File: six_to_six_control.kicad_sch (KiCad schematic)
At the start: 16 parts, among them J1 relays, J2 relays, J3 relays, J4 relays, J5 relays, J6 relays, J7 12V Power, U1 RS-485_module

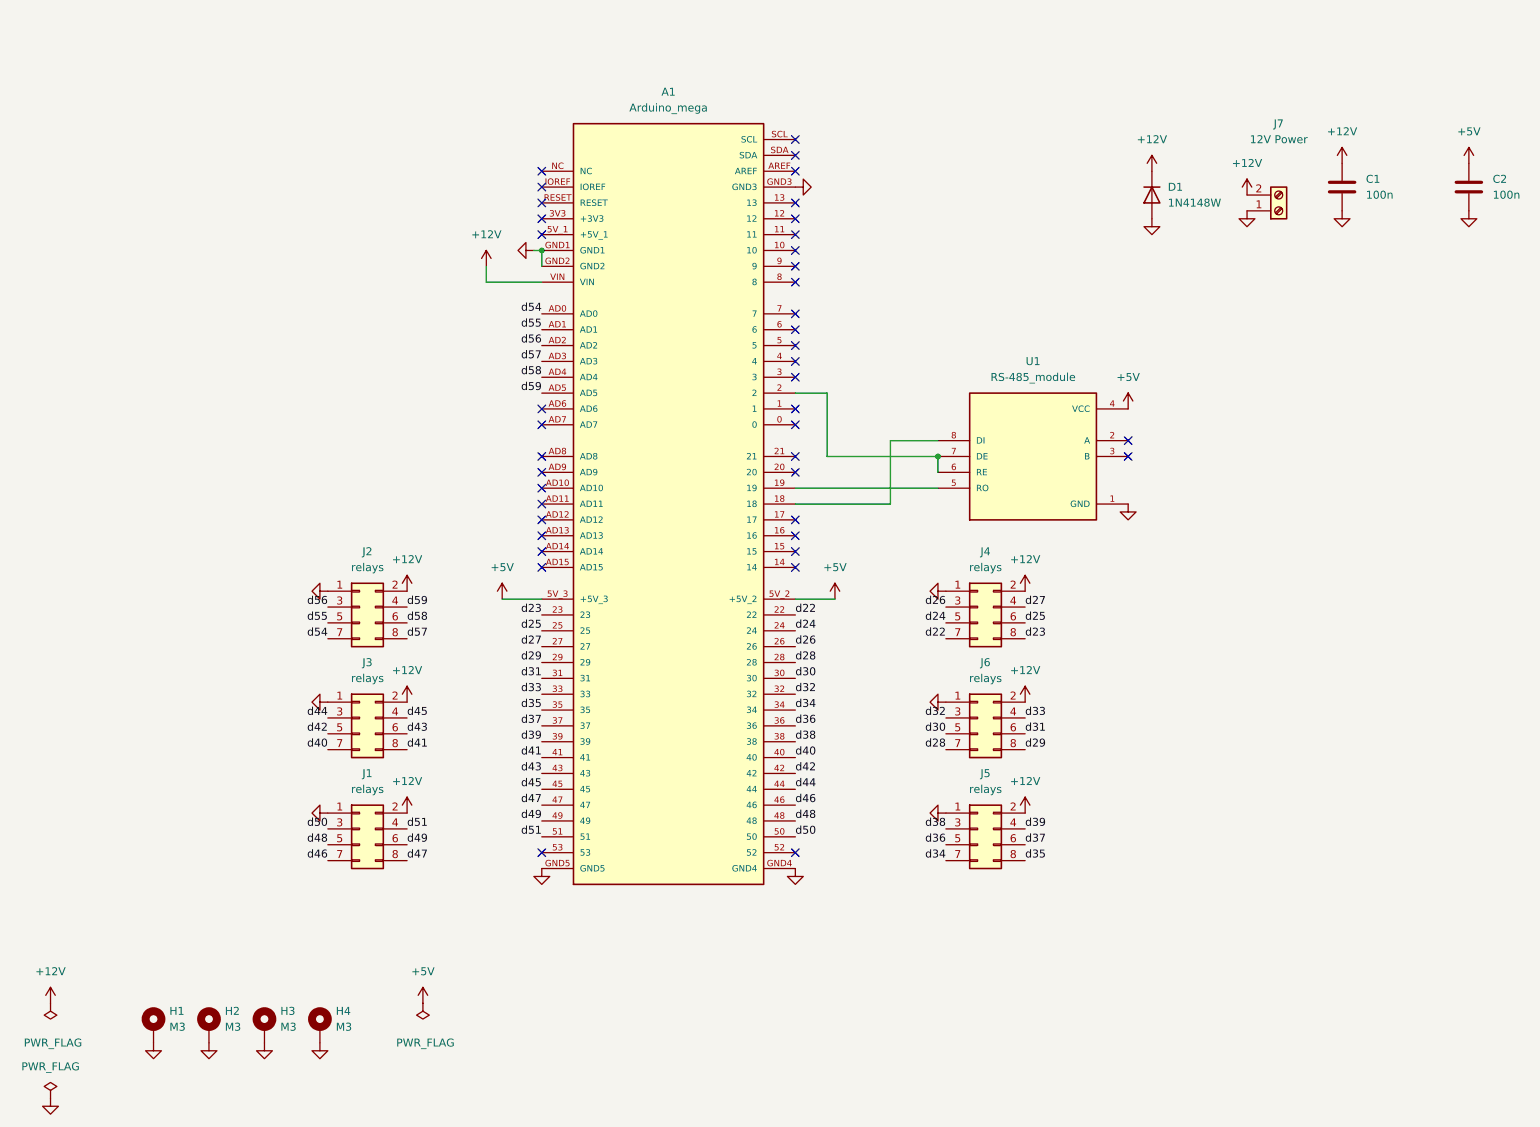
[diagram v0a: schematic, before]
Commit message: added db9 and Ethernet module
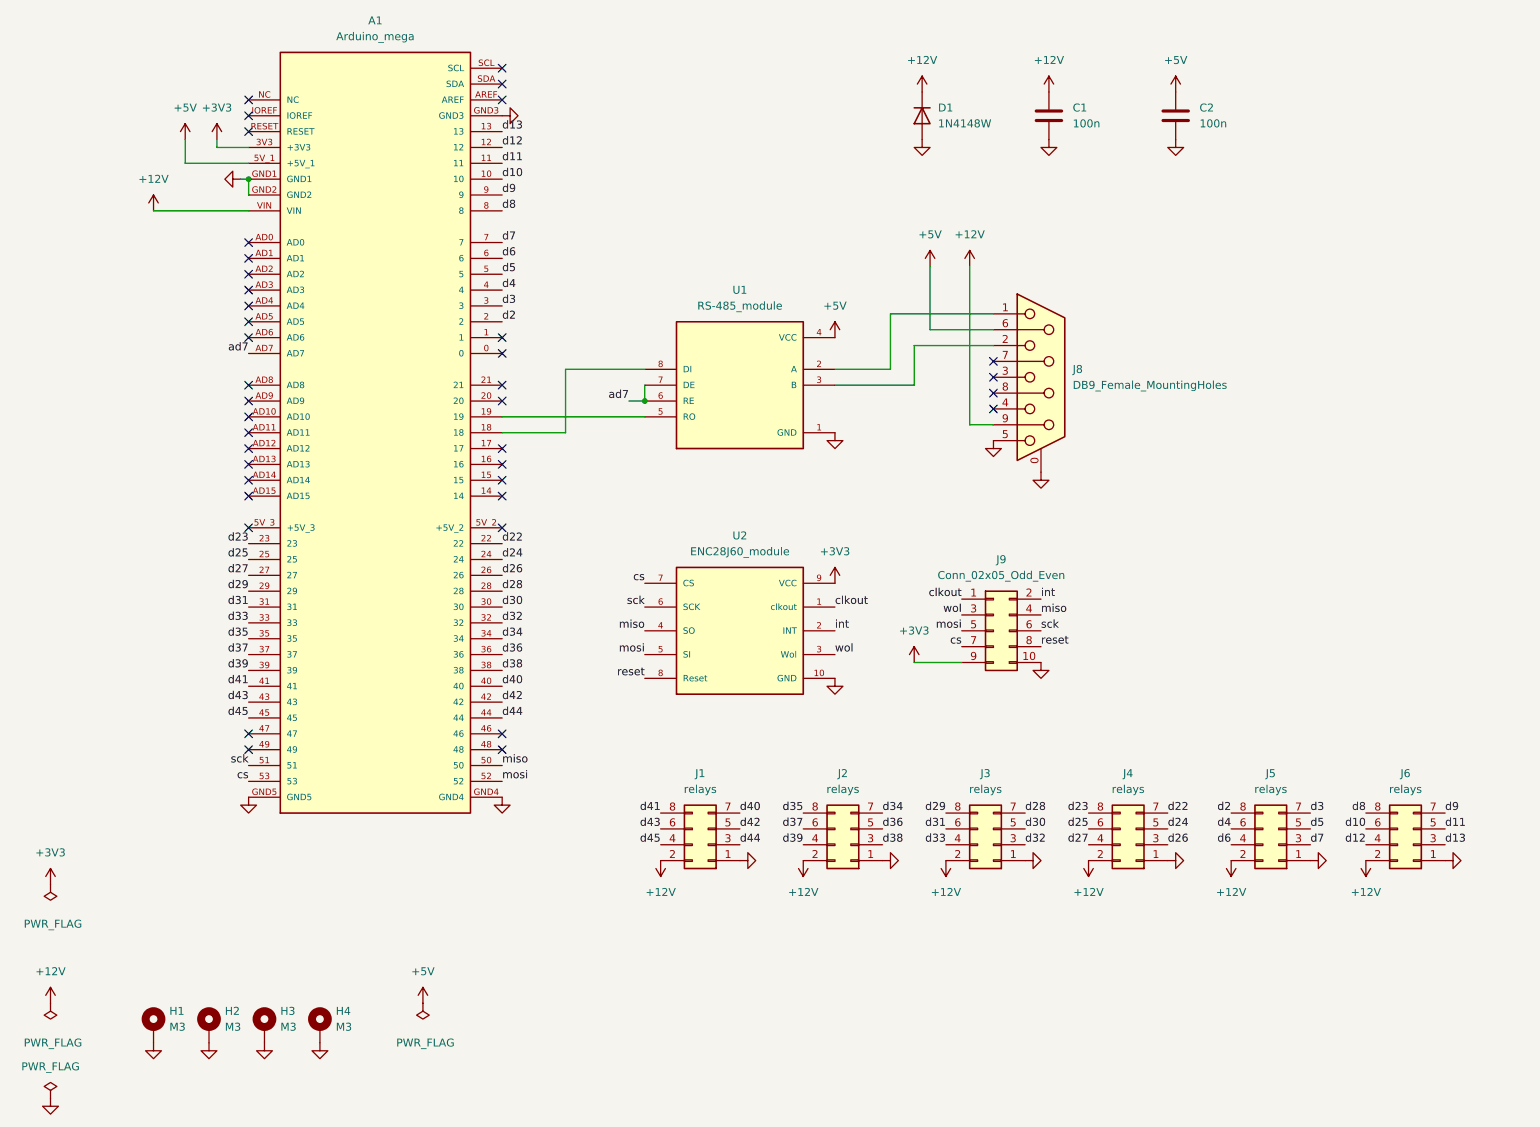
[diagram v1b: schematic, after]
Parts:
- removed J7: 12V Power, TerminalBlock_Phoenix:TerminalBlock_Phoenix_MKDS-1,5-2-5.08_1x02_P5.08mm_Horizontal, symbol Connector:Screw_Terminal_01x02
- added J8: DB9_Female_MountingHoles, Connector_Dsub:DSUB-9_Female_Horizontal_P2.77x2.84mm_EdgePinOffset9.90mm_Housed_MountingHolesOffset11.32mm, symbol Connector:DB9_Female_MountingHoles
- added J9: Conn_02x05_Odd_Even, Connector_PinHeader_2.54mm:PinHeader_2x05_P2.54mm_Vertical, symbol Connector_Generic:Conn_02x05_Odd_Even
- added U2: ENC28J60_module, Library:ENC28J60_module, symbol Library:ENC28J60_module
- renumbered J3 to J1, J5 to J2, J6 to J3, J1 to J5, J2 to J6
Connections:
- net +12V: now also J8.9
- net +5V: now also A1.5V_1 (+5V_1), J8.6; no longer A1.5V_2 (+5V_2), A1.5V_3 (+5V_3)
- net GND: now also J8.0 (PAD), J8.5, J9.10 (Pin_10), U2.10 (GND)
- net at U1.2 (A): now also J8.1
- net at U1.3 (B): now also J8.2
- net ad7: now reaches U1.6 (RE), U1.7 (DE)
- net ad7: now also A1.AD7; no longer A1.2
- net d10: now reaches A1.10
- net d10: now also J6.6 (Pin_6)
- net d11: now reaches A1.11
- net d11: now also J6.5 (Pin_5)
- net d12: now reaches A1.12
- net d12: now also J6.4 (Pin_4)
- net d13: now reaches A1.13
- net d13: now also J6.3 (Pin_3)
- net d3: now reaches A1.3
- net d3: now also J5.7 (Pin_7)
- net +3V3: now reaches A1.3V3 (+3V3)
- net +3V3: now also J9.9 (Pin_9), U2.9 (VCC)
- net d4: now reaches A1.4
- net d4: now also J5.6 (Pin_6)
- net d5: now reaches A1.5
- net d5: now also J5.5 (Pin_5)
- net mosi: now reaches A1.52
- net mosi: now also J9.5 (Pin_5), U2.5 (SI)
- net cs: now reaches A1.53
- net cs: now also J9.7 (Pin_7), U2.7 (CS)
- net d6: now reaches A1.6
- net d6: now also J5.4 (Pin_4)
- net d7: now reaches A1.7
- net d7: now also J5.3 (Pin_3)
- net d8: now reaches A1.8
- net d8: now also J6.8 (Pin_8)
- net d9: now reaches A1.9
- net d9: now also J6.7 (Pin_7)
- net d46: no longer names the net of A1.46
- net d46: no longer J5.7 (Pin_7)
- net d47: no longer names the net of A1.47
- net d47: no longer J5.8 (Pin_8)
- net d48: no longer names the net of A1.48
- net d48: no longer J5.5 (Pin_5)
- net d49: no longer names the net of A1.49
- net d49: no longer J5.6 (Pin_6)
- net d50 renamed miso
- net miso: now also J9.4 (Pin_4), U2.4 (SO); no longer J5.3 (Pin_3)
- net d51 renamed sck
- net sck: now also J9.6 (Pin_6), U2.6 (SCK); no longer J5.4 (Pin_4)
- net d54: no longer names the net of A1.AD0
- net d54: no longer J6.7 (Pin_7)
- net d55: no longer names the net of A1.AD1
- net d55: no longer J6.5 (Pin_5)
- net d56: no longer names the net of A1.AD2
- net d56: no longer J6.3 (Pin_3)
- net d57: no longer names the net of A1.AD3
- net d57: no longer J6.8 (Pin_8)
- net d58: no longer names the net of A1.AD4
- net d58: no longer J6.6 (Pin_6)
- net d59: no longer names the net of A1.AD5
- net d59: no longer J6.4 (Pin_4)
- new net clkout: J9.1 (Pin_1), U2.1 (clkout)
- new net d2: A1.2, J5.8 (Pin_8)
- new net int: J9.2 (Pin_2), U2.2 (INT)
- new net reset: J9.8 (Pin_8), U2.8 (Reset)
- new net wol: J9.3 (Pin_3), U2.3 (Wol)
- no-connect marks 41 -> 39
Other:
- moved on the sheet: A1, C1, C2, D1, J1, J2, J3, J4, J5, J6, U1

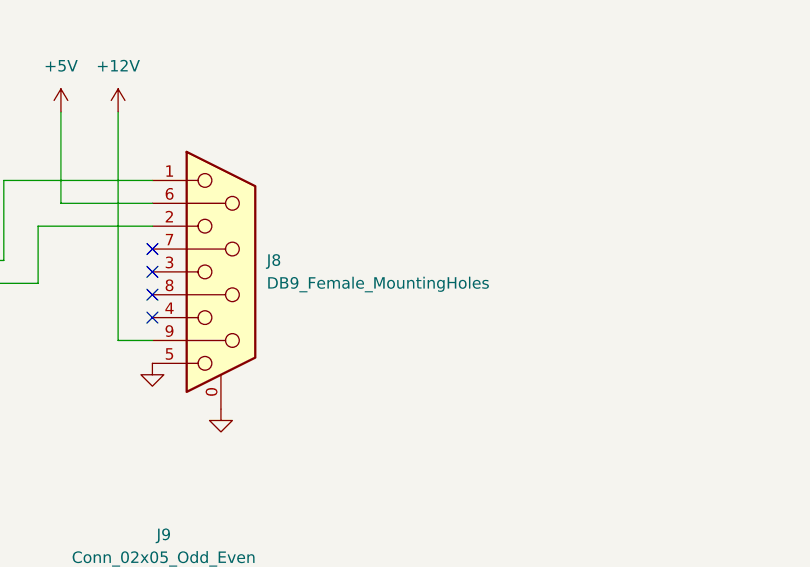
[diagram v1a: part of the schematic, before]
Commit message: fixed db9 layout
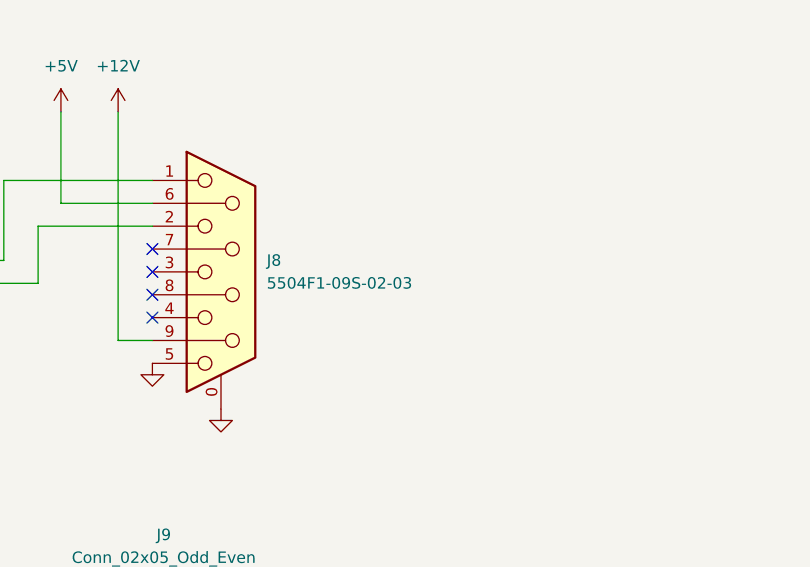
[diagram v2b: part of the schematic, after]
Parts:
- J8: value DB9_Female_MountingHoles -> 5504F1-09S-02-03; footprint Connector_Dsub:DSUB-9_Female_Horizontal_P2.77x2.84mm_EdgePinOffset9.90mm_Housed_MountingHolesOffset11.32mm -> Connector_Dsub:DSUB-9_Female_Horizontal_P2.77x2.84mm_EdgePinOffset7.70mm_Housed_MountingHolesOffset9.12mm
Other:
- title: (none) -> 6 on 6 Control
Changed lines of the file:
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@@
 (kicad_sch (version 20211123) (generator eeschema)
   (paper "A4")
+  (title_block
+    (title "6 on 6 Control")
+    (date "2023-03-28")
+    (rev "1.0")
+  )
   (junction (at 59.69 43.18) (diameter 0) (color 0 0 0 0)
   )
@@
       (effects (font (size 1.27 1.27)) (justify left))
     )
-    (property "Value" "DB9_Female_MountingHoles" (id 1) (at 191.77 76.1999 0)
+    (property "Value" "5504F1-09S-02-03" (id 1) (at 191.77 76.1999 0)
       (effects (font (size 1.27 1.27)) (justify left))
     )
-    (property "Footprint" "Connector_Dsub:DSUB-9_Female_Horizontal_P2.77x2.84mm_EdgePinOffset9.90mm_Housed_MountingHolesOffset11.32mm" (id 2) (at 186.69 74.93 0)
-      (effects (font (size 1.27 1.27)) hide)
-    )
-    (property "Datasheet" " ~" (id 3) (at 186.69 74.93 0)
+    (property "Footprint" "Connector_Dsub:DSUB-9_Female_Horizontal_P2.77x2.84mm_EdgePinOffset7.70mm_Housed_MountingHolesOffset9.12mm" (id 2) (at 186.69 74.93 0)
+      (effects (font (size 1.27 1.27)) hide)
+    )
+    (property "Datasheet" "https://www.ic-elect.si/fileuploader/download/download/?d=0&file=custom%2Fupload%2FFile-0-50476900-1473920528.pdf" (id 3) (at 186.69 74.93 0)
       (effects (font (size 1.27 1.27)) hide)
     )
@@
     )
     (path "/52333b97-d5d0-4767-8a42-4f99a2ede996"
-      (reference "J8") (unit 1) (value "DB9_Female_MountingHoles") (footprint "Connector_Dsub:DSUB-9_Female_Horizontal_P2.77x2.84mm_EdgePinOffset9.90mm_Housed_MountingHolesOffset11.32mm")
+      (reference "J8") (unit 1) (value "5504F1-09S-02-03") (footprint "Connector_Dsub:DSUB-9_Female_Horizontal_P2.77x2.84mm_EdgePinOffset7.70mm_Housed_MountingHolesOffset9.12mm")
     )
     (path "/f568ca57-4604-4095-a561-55f3b1417435"

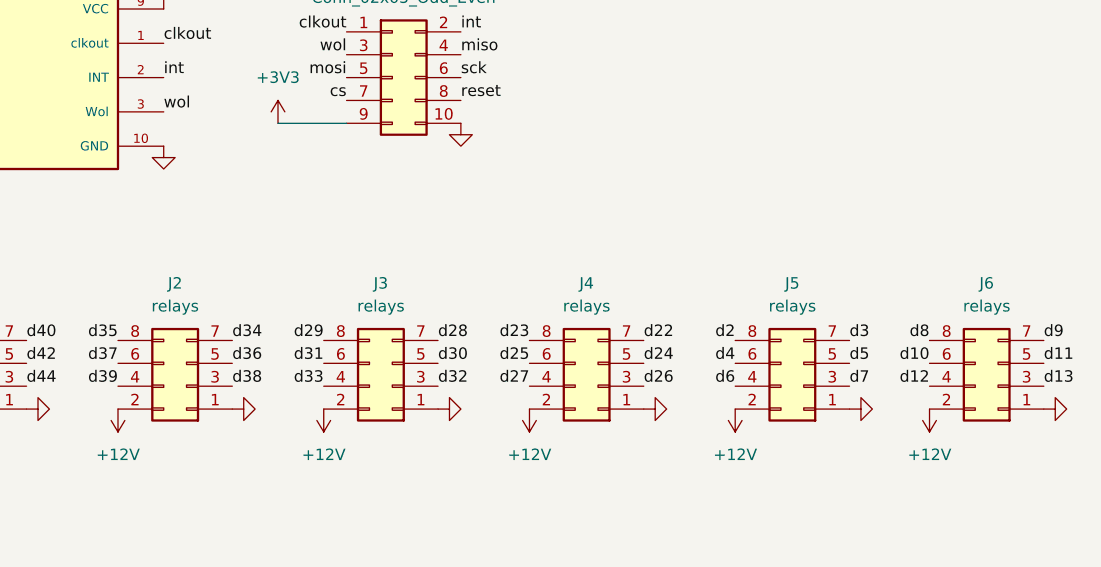
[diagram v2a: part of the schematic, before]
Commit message: reannotate connectors
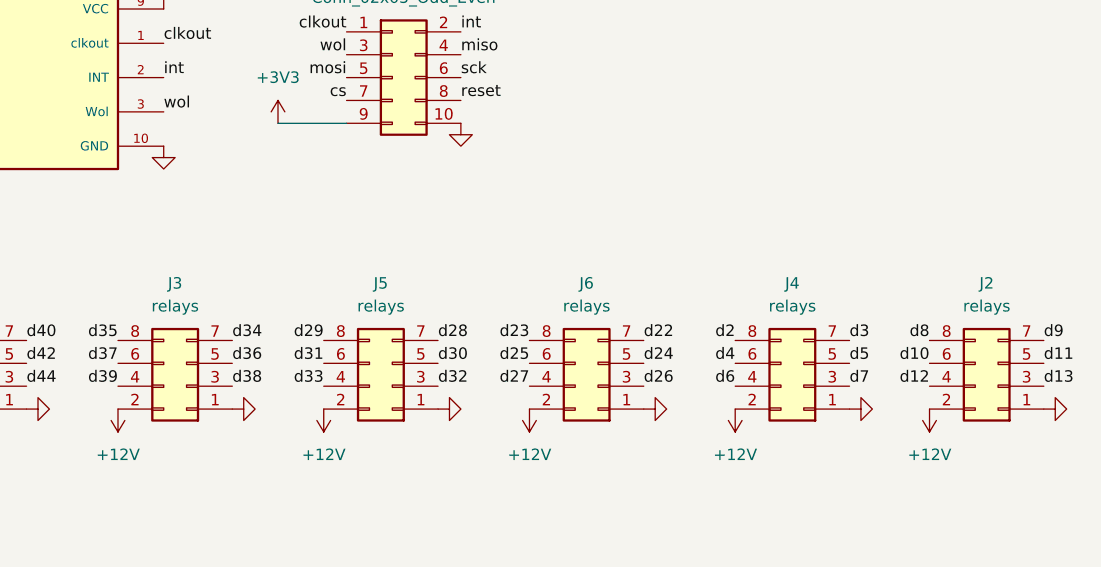
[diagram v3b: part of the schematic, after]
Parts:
- renumbered J6 to J2, J2 to J3, J5 to J4, J3 to J5, J4 to J6
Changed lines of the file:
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@@
   (symbol (lib_id "Connector_Generic:Conn_02x04_Odd_Even") (at 246.38 149.86 180) (unit 1)
     (in_bom yes) (on_board yes) (fields_autoplaced)
-    (property "Reference" "J6" (id 0) (at 245.11 138.43 0))
+    (property "Reference" "J2" (id 0) (at 245.11 138.43 0))
     (property "Value" "relays" (id 1) (at 245.11 140.97 0))
     (property "Footprint" "Connector_PinHeader_2.54mm:PinHeader_2x04_P2.54mm_Vertical" (id 2) (at 246.38 149.86 0)
@@
   (symbol (lib_id "Connector_Generic:Conn_02x04_Odd_Even") (at 156.21 149.86 180) (unit 1)
     (in_bom yes) (on_board yes)
-    (property "Reference" "J2" (id 0) (at 154.94 138.43 0))
+    (property "Reference" "J3" (id 0) (at 154.94 138.43 0))
     (property "Value" "relays" (id 1) (at 154.94 140.97 0))
     (property "Footprint" "Connector_PinHeader_2.54mm:PinHeader_2x04_P2.54mm_Vertical" (id 2) (at 156.21 149.86 0)
@@
   (symbol (lib_id "Connector_Generic:Conn_02x04_Odd_Even") (at 201.93 149.86 180) (unit 1)
     (in_bom yes) (on_board yes)
-    (property "Reference" "J4" (id 0) (at 200.66 138.43 0))
+    (property "Reference" "J6" (id 0) (at 200.66 138.43 0))
     (property "Value" "relays" (id 1) (at 200.66 140.97 0))
     (property "Footprint" "Connector_PinHeader_2.54mm:PinHeader_2x04_P2.54mm_Vertical" (id 2) (at 201.93 149.86 0)
@@
   (symbol (lib_id "Connector_Generic:Conn_02x04_Odd_Even") (at 224.79 149.86 180) (unit 1)
     (in_bom yes) (on_board yes) (fields_autoplaced)
-    (property "Reference" "J5" (id 0) (at 223.52 138.43 0))
+    (property "Reference" "J4" (id 0) (at 223.52 138.43 0))
     (property "Value" "relays" (id 1) (at 223.52 140.97 0))
     (property "Footprint" "Connector_PinHeader_2.54mm:PinHeader_2x04_P2.54mm_Vertical" (id 2) (at 224.79 149.86 0)
@@
   (symbol (lib_id "Connector_Generic:Conn_02x04_Odd_Even") (at 179.07 149.86 180) (unit 1)
     (in_bom yes) (on_board yes) (fields_autoplaced)
-    (property "Reference" "J3" (id 0) (at 177.8 138.43 0))
+    (property "Reference" "J5" (id 0) (at 177.8 138.43 0))
     (property "Value" "relays" (id 1) (at 177.8 140.97 0))
     (property "Footprint" "Connector_PinHeader_2.54mm:PinHeader_2x04_P2.54mm_Vertical" (id 2) (at 179.07 149.86 0)
@@
       (reference "J1") (unit 1) (value "relays") (footprint "Connector_PinHeader_2.54mm:PinHeader_2x04_P2.54mm_Vertical")
     )
+    (path "/3ae82406-901b-4872-873c-60c7d5433f2b"
+      (reference "J2") (unit 1) (value "relays") (footprint "Connector_PinHeader_2.54mm:PinHeader_2x04_P2.54mm_Vertical")
+    )
     (path "/65b3bfbb-e1a3-4499-b651-549304f2a721"
-      (reference "J2") (unit 1) (value "relays") (footprint "Connector_PinHeader_2.54mm:PinHeader_2x04_P2.54mm_Vertical")
+      (reference "J3") (unit 1) (value "relays") (footprint "Connector_PinHeader_2.54mm:PinHeader_2x04_P2.54mm_Vertical")
+    )
+    (path "/74ce509c-1da2-4877-9348-3a57506aac8a"
+      (reference "J4") (unit 1) (value "relays") (footprint "Connector_PinHeader_2.54mm:PinHeader_2x04_P2.54mm_Vertical")
     )
     (path "/ad83ee7d-79d9-4dfd-b738-b9e7f4e9151a"
-      (reference "J3") (unit 1) (value "relays") (footprint "Connector_PinHeader_2.54mm:PinHeader_2x04_P2.54mm_Vertical")
+      (reference "J5") (unit 1) (value "relays") (footprint "Connector_PinHeader_2.54mm:PinHeader_2x04_P2.54mm_Vertical")
     )
     (path "/746d59ff-6954-41c0-a411-57fbdda7a9da"
-      (reference "J4") (unit 1) (value "relays") (footprint "Connector_PinHeader_2.54mm:PinHeader_2x04_P2.54mm_Vertical")
-    )
-    (path "/74ce509c-1da2-4877-9348-3a57506aac8a"
-      (reference "J5") (unit 1) (value "relays") (footprint "Connector_PinHeader_2.54mm:PinHeader_2x04_P2.54mm_Vertical")
-    )
-    (path "/3ae82406-901b-4872-873c-60c7d5433f2b"
       (reference "J6") (unit 1) (value "relays") (footprint "Connector_PinHeader_2.54mm:PinHeader_2x04_P2.54mm_Vertical")
     )
